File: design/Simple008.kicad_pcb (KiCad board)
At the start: 4 copper layers, 100 x 100 mm, 43 parts, among them IC1 DS1233-10+, J1 UART A, J2 UART B, J3 SD CARD, J4 Power, J5 ATF1508 JTAG, SW1 SW_Push, U1 SST39SF040, U2 AS6C8008-55ZIN, U3 MC68008, U4 XR68C681, U5 ATF1508, U6 AS6C8008-55ZIN, U7 AS6C8008-55ZIN, U8 AS6C8008-55ZIN, Y1 10MHz, Y2 3.6864MHz

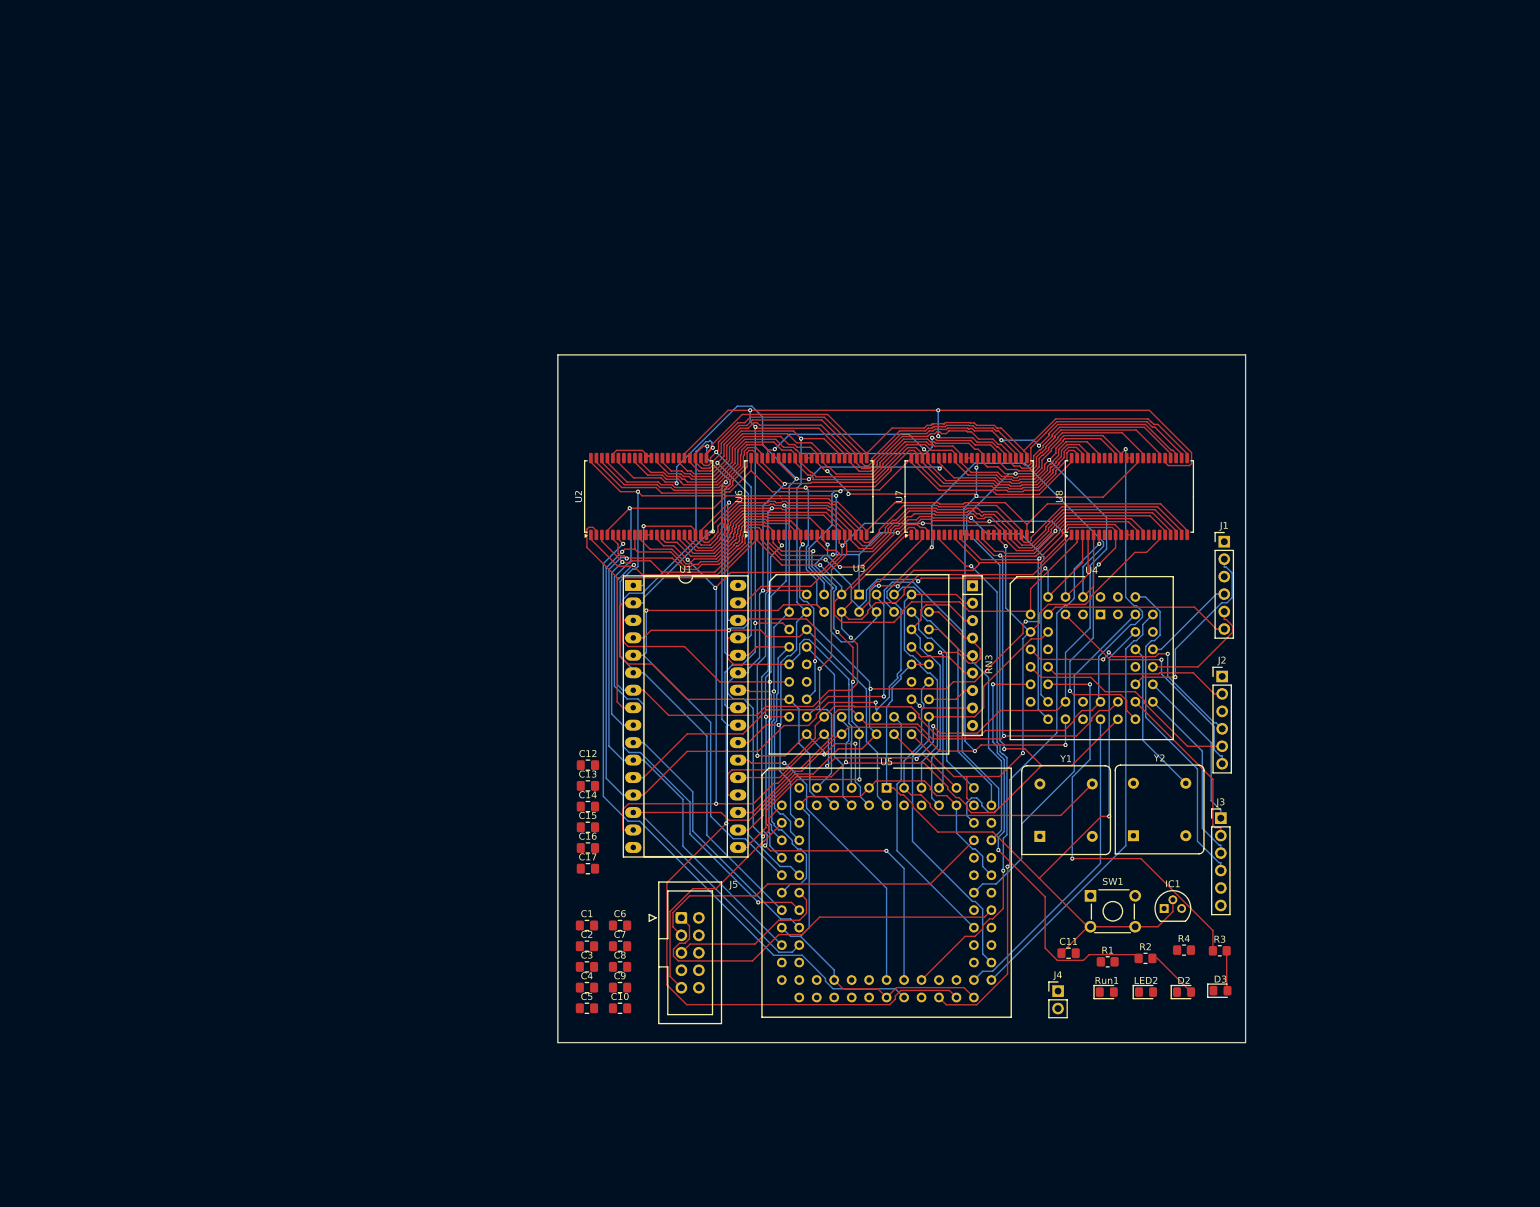
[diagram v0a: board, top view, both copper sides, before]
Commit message: PCB layout component positioning
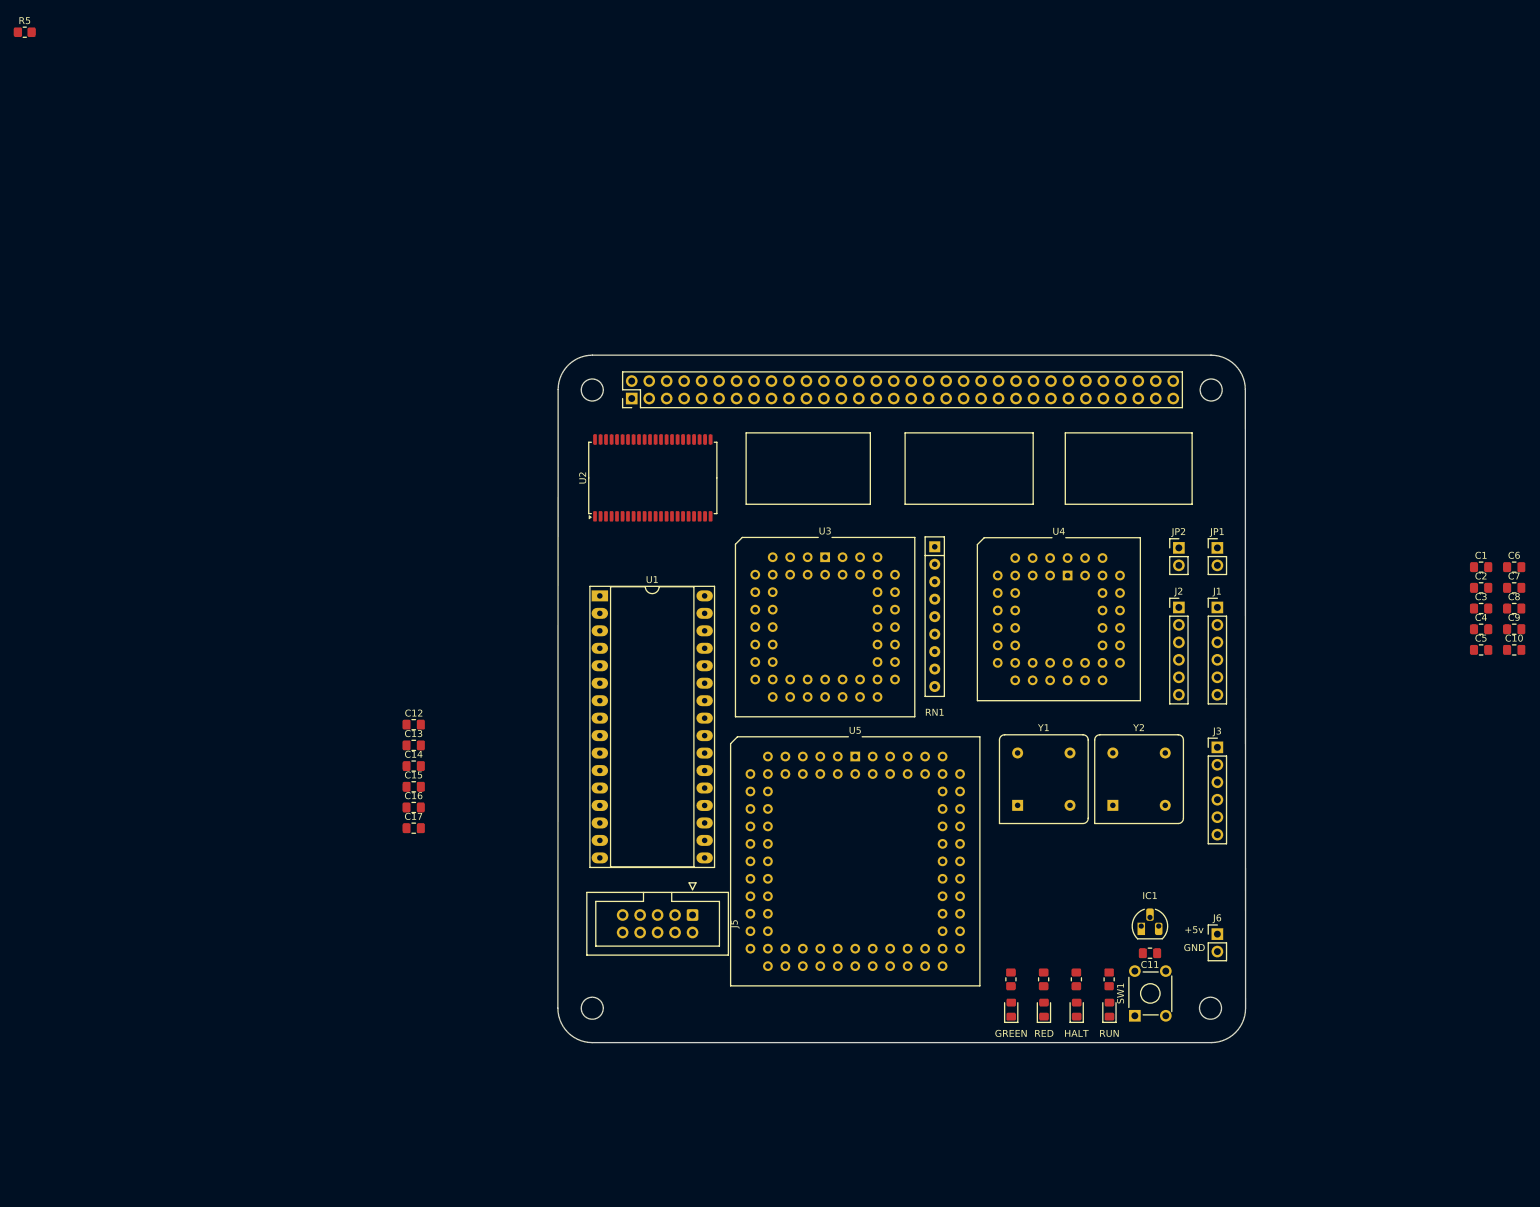
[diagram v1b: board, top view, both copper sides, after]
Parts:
- removed D2, Run1: RED, LED_SMD:LED_0805_2012Metric_Pad1.15x1.40mm_HandSolder
- removed D3: GREEN, LED_SMD:LED_0805_2012Metric_Pad1.15x1.40mm_HandSolder
- removed RN3: R_Network08_Split, Resistor_THT:R_Array_SIP9
- removed U6, U7, U8: AS6C8008-55ZIN, Package_SO:TSOP-II-44_10.16x18.41mm_P0.8mm
- added H1: MountingHole, MountingHole:MountingHole_3.2mm_M3, F.Cu at (84.4, 53.0)
- added H2: MountingHole, MountingHole:MountingHole_3.2mm_M3, F.Cu at (174.4, 53.0)
- added H3: MountingHole, MountingHole:MountingHole_3.2mm_M3, F.Cu at (84.4, 142.9)
- added H4: MountingHole, MountingHole:MountingHole_3.2mm_M3, F.Cu at (174.3, 142.9)
- added J6: Conn_01x02_Pin, Connector_PinHeader_2.54mm:PinHeader_1x02_P2.54mm_Vertical, F.Cu at (175.3, 132.1)
- added JP1: Power A, Connector_PinHeader_2.54mm:PinHeader_1x02_P2.54mm_Vertical, F.Cu at (175.3, 76.0)
- added JP2: Power B, Connector_PinHeader_2.54mm:PinHeader_1x02_P2.54mm_Vertical, F.Cu at (169.7, 76.0)
- added LED1: GREEN, LED_SMD:LED_0805_2012Metric_Pad1.15x1.40mm_HandSolder, F.Cu at (145.3, 143.1)
- added LED3: HALT, LED_SMD:LED_0805_2012Metric_Pad1.15x1.40mm_HandSolder, F.Cu at (154.8, 143.1)
- added LED4: RUN, LED_SMD:LED_0805_2012Metric_Pad1.15x1.40mm_HandSolder, F.Cu at (159.6, 143.1)
- added R5: 10K, Resistor_SMD:R_0805_2012Metric_Pad1.20x1.40mm_HandSolder, F.Cu at (1.88, 0.97)
- added RN1: R_Network08, Resistor_THT:R_Array_SIP9, F.Cu at (134.2, 75.8)
- IC1: footprint Package_TO_SOT_THT:TO-92 -> Package_TO_SOT_THT:TO-92_HandSolder
- J4: value Power -> Conn_02x32_Odd_Even; footprint Connector_PinHeader_2.54mm:PinHeader_1x02_P2.54mm_Vertical -> Connector_PinHeader_2.54mm:PinHeader_2x32_P2.54mm_Vertical
- LED2: value Halt -> RED
- moved C1 140.1 mm to (213.7, 78.8)
- moved C10 140.1 mm to (218.5, 90.8)
- moved C2 140.1 mm to (213.7, 81.8)
- moved C3 140.1 mm to (213.7, 84.8)
- moved C4 140.1 mm to (213.7, 87.8)
- moved C5 140.1 mm to (213.7, 90.8)
- moved C6 140.1 mm to (218.5, 78.8)
- moved C7 140.1 mm to (218.5, 81.8)
- moved C8 140.1 mm to (218.5, 84.8)
- moved C9 140.1 mm to (218.5, 87.8)
- moved J4 106.1 mm to (90.1, 54.2), turned to 90 degrees
- moved C12 26.0 mm to (58.4, 101.7)
- moved C14 26.0 mm to (58.4, 107.7)
- moved C15 26.0 mm to (58.4, 110.7)
- moved C16 26.0 mm to (58.4, 113.7)
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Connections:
- C1 pad 1: +5V -> Net-(C1-Pad1)
- C1 pad 2: +5V -> Net-(C1-Pad1)
- C10 pad 1: +5V -> Net-(C1-Pad1)
- C10 pad 2: +5V -> Net-(C1-Pad1)
- C11 pad 2: +5V -> GND
- C12 pad 1: +5V -> Net-(C12-Pad1)
- C12 pad 2: +5V -> Net-(C12-Pad1)
- C13 pad 1: +5V -> Net-(C12-Pad1)
- C13 pad 2: +5V -> Net-(C12-Pad1)
- C14 pad 1: +5V -> Net-(C12-Pad1)
- C14 pad 2: +5V -> Net-(C12-Pad1)
- C15 pad 1: +5V -> Net-(C12-Pad1)
- C15 pad 2: +5V -> Net-(C12-Pad1)
- C16 pad 1: +5V -> Net-(C12-Pad1)
- C16 pad 2: +5V -> Net-(C12-Pad1)
- C17 pad 1: +5V -> Net-(C12-Pad1)
- C17 pad 2: +5V -> Net-(C12-Pad1)
- C2 pad 1: +5V -> Net-(C1-Pad1)
- C2 pad 2: +5V -> Net-(C1-Pad1)
- C3 pad 1: +5V -> Net-(C1-Pad1)
- C3 pad 2: +5V -> Net-(C1-Pad1)
- C4 pad 1: +5V -> Net-(C1-Pad1)
- C4 pad 2: +5V -> Net-(C1-Pad1)
- C5 pad 1: +5V -> Net-(C1-Pad1)
- C5 pad 2: +5V -> Net-(C1-Pad1)
- C6 pad 1: +5V -> Net-(C1-Pad1)
- C6 pad 2: +5V -> Net-(C1-Pad1)
- C7 pad 1: +5V -> Net-(C1-Pad1)
- C7 pad 2: +5V -> Net-(C1-Pad1)
- C8 pad 1: +5V -> Net-(C1-Pad1)
- C8 pad 2: +5V -> Net-(C1-Pad1)
- C9 pad 1: +5V -> Net-(C1-Pad1)
- C9 pad 2: +5V -> Net-(C1-Pad1)
- IC1 pad 1: +5V -> GND
- IC1 pad 3: +5V -> VCC
- J1 pad 1: +5V -> GND
- J2 pad 1: +5V -> GND
- J3 pad 5: +5V -> VCC
- J3 pad 6: +5V -> GND
- J4 pad 1: +5V -> A0
- J4 pad 2: +5V -> VCC
- J5 pad 10: +5V -> GND
- J5 pad 2: +5V -> GND
- LED2 pad 1: (no net) -> GND
- LED2 pad 2: (no net) -> Net-(LED2-A)
- R1 pad 1: Net-(R1-Pad1) -> VCC
- R1 pad 2: +5V -> Net-(LED3-A)
- R2 pad 1: Net-(U4-OP3) -> Net-(U4-OP5)
- R3 pad 1: Net-(U4-OP5) -> Net-(U4-OP3)
- R3 pad 2: Net-(D3-A) -> Net-(LED2-A)
- R4 pad 1: Net-(LED2-PadA) -> HALT
- R4 pad 2: +5V -> Net-(LED4-A)
- SW1 pad 1: +5V -> GND
- U1 pad 16: +5V -> GND
- U1 pad 32: +5V -> VCC
- U2 pad 11: +5V -> VCC
- U2 pad 12: +5V -> GND
- U2 pad 33: +5V -> VCC
- U2 pad 34: +5V -> GND
- U2 pad 40: +5V -> VCC
- U3 pad 15: +5V -> VCC
- U3 pad 17: +5V -> GND
- U3 pad 39: +5V -> GND
- U4 pad 17: SPICS2 -> unconnected-(U4-OP7-Pad17)
- U4 pad 22: +5V -> GND
- U4 pad 3: +5V -> GND
- U4 pad 42: +5V -> GND
- U4 pad 43: +5V -> GND
- U4 pad 44: +5V -> VCC
- U5 pad 19: +5V -> GND
- U5 pad 32: +5V -> GND
- U5 pad 35: unconnected-(U5-I/O-Pad35) -> GPIO0
- U5 pad 36: unconnected-(U5-I/O-Pad36) -> GPIO1
- U5 pad 37: unconnected-(U5-I/O-Pad37) -> GPIO2
- U5 pad 39: unconnected-(U5-I/O-Pad39) -> GPIO3
- U5 pad 40: unconnected-(U5-I/O-Pad40) -> GPIO4
- U5 pad 41: unconnected-(U5-I/O-Pad41) -> GPIO5
- U5 pad 42: +5V -> GND
- U5 pad 47: +5V -> GND
- U5 pad 52: unconnected-(U5-I/O-Pad52) -> GPIO6
- U5 pad 57: unconnected-(U5-I/O-Pad57) -> GPIO7
- U5 pad 59: +5V -> GND
- U5 pad 7: +5V -> GND
- U5 pad 72: +5V -> GND
- U5 pad 82: +5V -> GND
- U5 pad 84: OE1/I -> unconnected-(U5-OE1/I-Pad84)
- Y1 pad 4: +5V -> GND
- Y1 pad 8: +5V -> VCC
- Y2 pad 4: +5V -> GND
- Y2 pad 8: +5V -> VCC
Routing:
- net D4: track 217.1 -> 0.00 mm, vias 3 -> 0
- net D0: track 217.0 -> 0.00 mm, vias 5 -> 0
- net D2: track 211.9 -> 0.00 mm, vias 5 -> 0
- net WR: track 210.8 -> 0.00 mm, vias 4 -> 0
- net A1: track 205.7 -> 0.00 mm, vias 4 -> 0
- net A11: track 199.3 -> 0.00 mm, vias 5 -> 0
- net D6: track 199.1 -> 0.00 mm, vias 1 -> 0
- net A2: track 197.2 -> 0.00 mm, vias 5 -> 0
- net D7: track 191.0 -> 0.00 mm, vias 4 -> 0
- net D1: track 187.8 -> 0.00 mm, vias 4 -> 0
- net D5: track 185.0 -> 0.00 mm, vias 6 -> 0
- net D3: track 185.0 -> 0.00 mm, vias 7 -> 0
- net A7: track 184.9 -> 0.00 mm, vias 2 -> 0
- net A3: track 180.7 -> 0.00 mm, vias 5 -> 0
- net A15: track 178.4 -> 0.00 mm, vias 2 -> 0
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- added copper zone on In1.Cu, net GND
- added copper zone on In2.Cu, net VCC
- removed copper zone on In1.Cu, net +5V
- removed copper zone on In2.Cu, net +5V
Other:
- outline, holes or cut-outs redrawn
- board text added: "+5v"
- board text added: "GND"

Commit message: Initial board routing
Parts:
- added C20: 470uF, Capacitor_THT:CP_Radial_D10.0mm_P3.50mm, F.Cu at (171.4, 99.7)
- added C21: 100uF, Capacitor_THT:CP_Radial_D5.0mm_P2.50mm, F.Cu at (164.3, 95.6)
- C8, C9: moved to B.Cu
- moved R5 164.2 mm to (90.4, 139.3)
- moved C8 127.4 mm to (93.1, 61.7), turned to 180 degrees
- moved C9 126.7 mm to (93.2, 68.8)
- moved C10 121.3 mm to (101.9, 124.2), turned to 180 degrees
- moved C1 113.3 mm to (100.4, 80.3), turned to 180 degrees
- moved C4 110.2 mm to (103.5, 88.7), turned to -90 degrees
- moved C6 108.3 mm to (112.7, 101.9)
- moved C7 99.5 mm to (121.0, 101.9)
- moved J3 98.6 mm to (91.8, 52.5), turned to 90 degrees
- moved J4 90.6 mm to (89.8, 144.8)
- moved C13 85.2 mm to (142.2, 120.0), turned to -90 degrees
- moved C2 69.4 mm to (147.2, 101.8)
- moved C5 64.2 mm to (152.0, 72.9)
- moved JP2 59.3 mm to (115.2, 52.5), turned to 90 degrees
- moved C14 58.5 mm to (39.5, 163.0)
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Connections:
- C1 pad 1: Net-(C1-Pad1) -> VCC
- C1 pad 2: Net-(C1-Pad1) -> GND
- C10 pad 1: Net-(C1-Pad1) -> VCC
- C10 pad 2: Net-(C1-Pad1) -> GND
- C12 pad 1: Net-(C12-Pad1) -> VCC
- C12 pad 2: Net-(C12-Pad1) -> GND
- C13 pad 1: Net-(C12-Pad1) -> VCC
- C13 pad 2: Net-(C12-Pad1) -> GND
- C14 pad 1: Net-(C12-Pad1) -> VCC
- C14 pad 2: Net-(C12-Pad1) -> GND
- C15 pad 1: Net-(C12-Pad1) -> VCC
- C15 pad 2: Net-(C12-Pad1) -> GND
- C16 pad 1: Net-(C12-Pad1) -> VCC
- C16 pad 2: Net-(C12-Pad1) -> GND
- C17 pad 1: Net-(C12-Pad1) -> VCC
- C17 pad 2: Net-(C12-Pad1) -> GND
- C2 pad 1: Net-(C1-Pad1) -> VCC
- C2 pad 2: Net-(C1-Pad1) -> GND
- C3 pad 1: Net-(C1-Pad1) -> VCC
- C3 pad 2: Net-(C1-Pad1) -> GND
- C4 pad 1: Net-(C1-Pad1) -> VCC
- C4 pad 2: Net-(C1-Pad1) -> GND
- C5 pad 1: Net-(C1-Pad1) -> VCC
- C5 pad 2: Net-(C1-Pad1) -> GND
- C6 pad 1: Net-(C1-Pad1) -> VCC
- C6 pad 2: Net-(C1-Pad1) -> GND
- C7 pad 1: Net-(C1-Pad1) -> VCC
- C7 pad 2: Net-(C1-Pad1) -> GND
- C8 pad 1: Net-(C1-Pad1) -> VCC
- C8 pad 2: Net-(C1-Pad1) -> GND
- C9 pad 1: Net-(C1-Pad1) -> VCC
- C9 pad 2: Net-(C1-Pad1) -> GND
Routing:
- net D0: track 0.00 -> 229.9 mm, vias 0 -> 1
- net D1: track 0.00 -> 193.9 mm, vias 0 -> 5
- net HALT: track 0.00 -> 190.5 mm, vias 0 -> 2
- net D5: track 0.00 -> 186.6 mm, vias 0 -> 6
- net D6: track 0.00 -> 186.5 mm, vias 0 -> 4
- net D2: track 0.00 -> 182.8 mm, vias 0 -> 2
- net A1: track 0.00 -> 180.2 mm
- net D4: track 0.00 -> 174.8 mm, vias 0 -> 2
- net A15: track 0.00 -> 174.2 mm, vias 0 -> 2
- net A3: track 0.00 -> 171.0 mm, vias 0 -> 4
- net D3: track 0.00 -> 170.2 mm, vias 0 -> 3
- net D7: track 0.00 -> 169.8 mm, vias 0 -> 2
- net A2: track 0.00 -> 168.8 mm, vias 0 -> 2
- net A0: track 0.00 -> 166.0 mm
- net RW: track 0.00 -> 161.2 mm, vias 0 -> 2
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
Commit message: Clean ERC
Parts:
- removed C14, C15, C16, C17: 100uF, Capacitor_SMD:C_0805_2012Metric_Pad1.18x1.45mm_HandSolder
- moved C21 0.45 mm to (163.9, 95.4)

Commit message: Fabrication
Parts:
- added J7: USB_C_Receptacle_PowerOnly_6P, Connector_USB:USB_C_Receptacle_GCT_USB4125-xx-x_6P_TopMnt_Horizontal, F.Cu at (175.5, 110.5)
- added R6: 5K1, Resistor_SMD:R_0805_2012Metric_Pad1.20x1.40mm_HandSolder, F.Cu at (164.0, 112.0)
- added R7: 5K1, Resistor_SMD:R_0805_2012Metric_Pad1.20x1.40mm_HandSolder, F.Cu at (164.0, 109.0)
- added U6: TPS22929D, Package_TO_SOT_SMD:SOT-23-6, F.Cu at (168.6, 102.0)
- H1, H2, H3, H4: value MountingHole -> MountingHole_Pad; footprint MountingHole:MountingHole_3.2mm_M3 -> MountingHole:MountingHole_3.2mm_M3_Pad_Via
- moved J6 7.68 mm to (176.8, 100.3)
- moved C20 6.22 mm to (170.9, 93.5)
- moved C21 3.03 mm to (163.0, 92.5)
- moved C3 2.50 mm to (167.4, 73.2)
- moved Y2 2.50 mm to (166.5, 84.7)
- moved RESET 2.23 mm to (177.2, 122.0)
- moved IC1 2.10 mm to (164.2, 121.2)
- moved C11 2.10 mm to (167.4, 120.0)
- moved H4 0.10 mm to (174.4, 142.9)
- moved H1 0.06 mm to (84.4, 52.9)
- moved H2 0.06 mm to (174.4, 52.9)
- renumbered SW1 to RESET
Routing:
- net Net-(U6-ON): track 0.00 -> 17.3 mm
- net GND: track 28.8 -> 41.8 mm, vias 13 -> 16
- net Net-(J7-CC1): track 0.00 -> 7.83 mm
- net Net-(J7-CC2): track 0.00 -> 7.81 mm
- net VCC: track 20.9 -> 23.0 mm, vias 15 -> 16
- net HALT: track 190.5 -> 192.6 mm
- net A0: track 166.0 -> 168.0 mm
- net Net-(U4-X1/CLK): track 22.0 -> 23.7 mm
- net TDO: track 46.4 -> 48.1 mm
- net RAMSEL1: track 131.5 -> 132.9 mm
- net CLK: track 124.1 -> 125.3 mm
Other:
- board text added: "SD CARD"
- board text added: "Simple008 Malcolm Harrow, February 2025, v1 https://www.github.com/harrowm/Simple008"
- board text added: "UART A"
- board text added: "UART B"
